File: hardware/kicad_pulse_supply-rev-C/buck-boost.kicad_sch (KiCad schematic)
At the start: 32 parts, among them U12 TPS552892RYQR

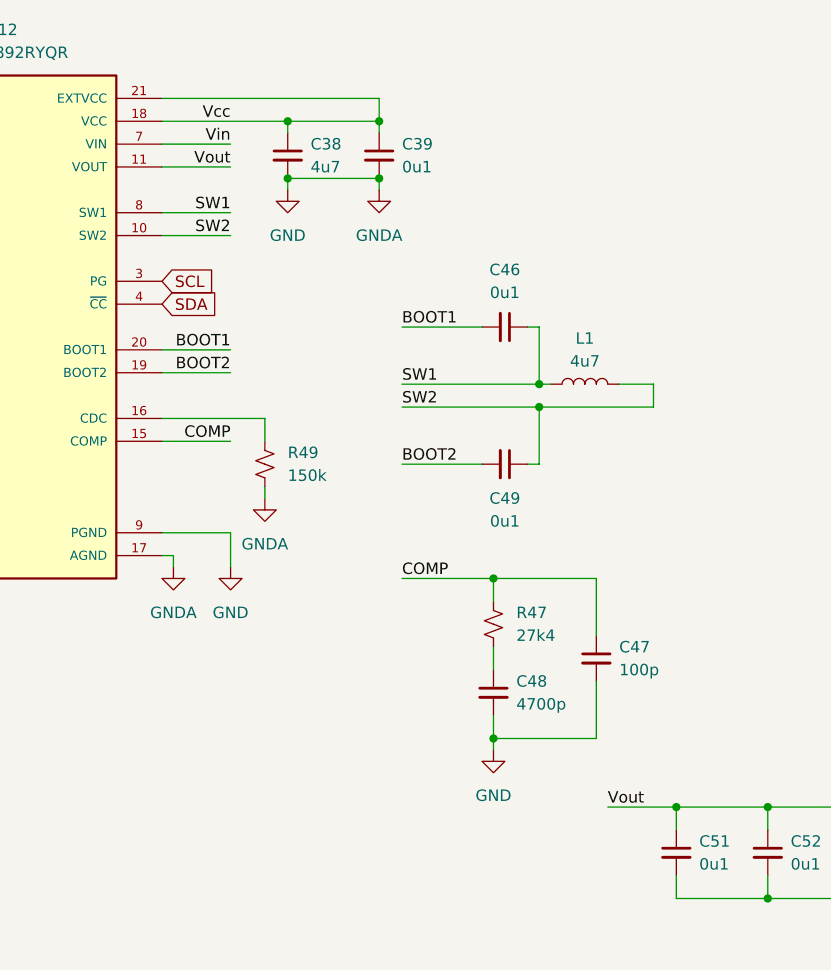
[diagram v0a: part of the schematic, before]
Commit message: Refactored main loop to use Arduino Strings
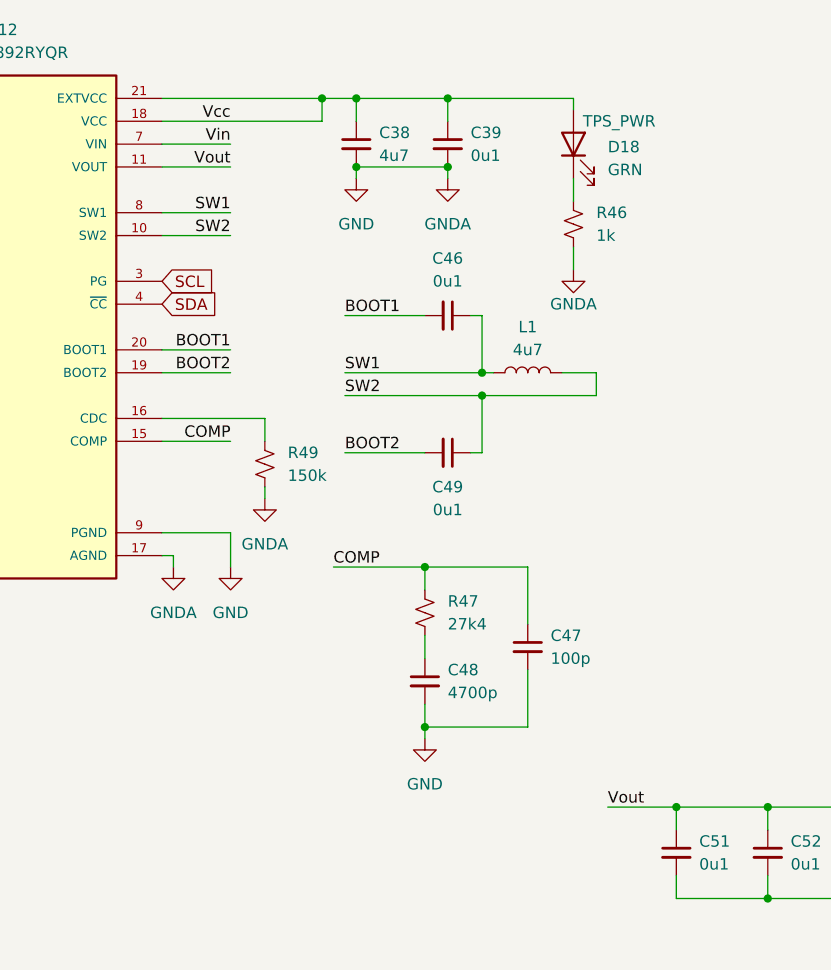
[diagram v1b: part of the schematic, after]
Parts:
- added D18: GRN, symbol Device:LED
- added R46: 1k, symbol Device:R_Small_US
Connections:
- net GND: now also R46.2
- net Vcc: now also D18.2 (A)
- new net: D18.1 (K), R46.1
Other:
- moved on the sheet: C38, C39, C46, C47, C48, C49, L1, R47

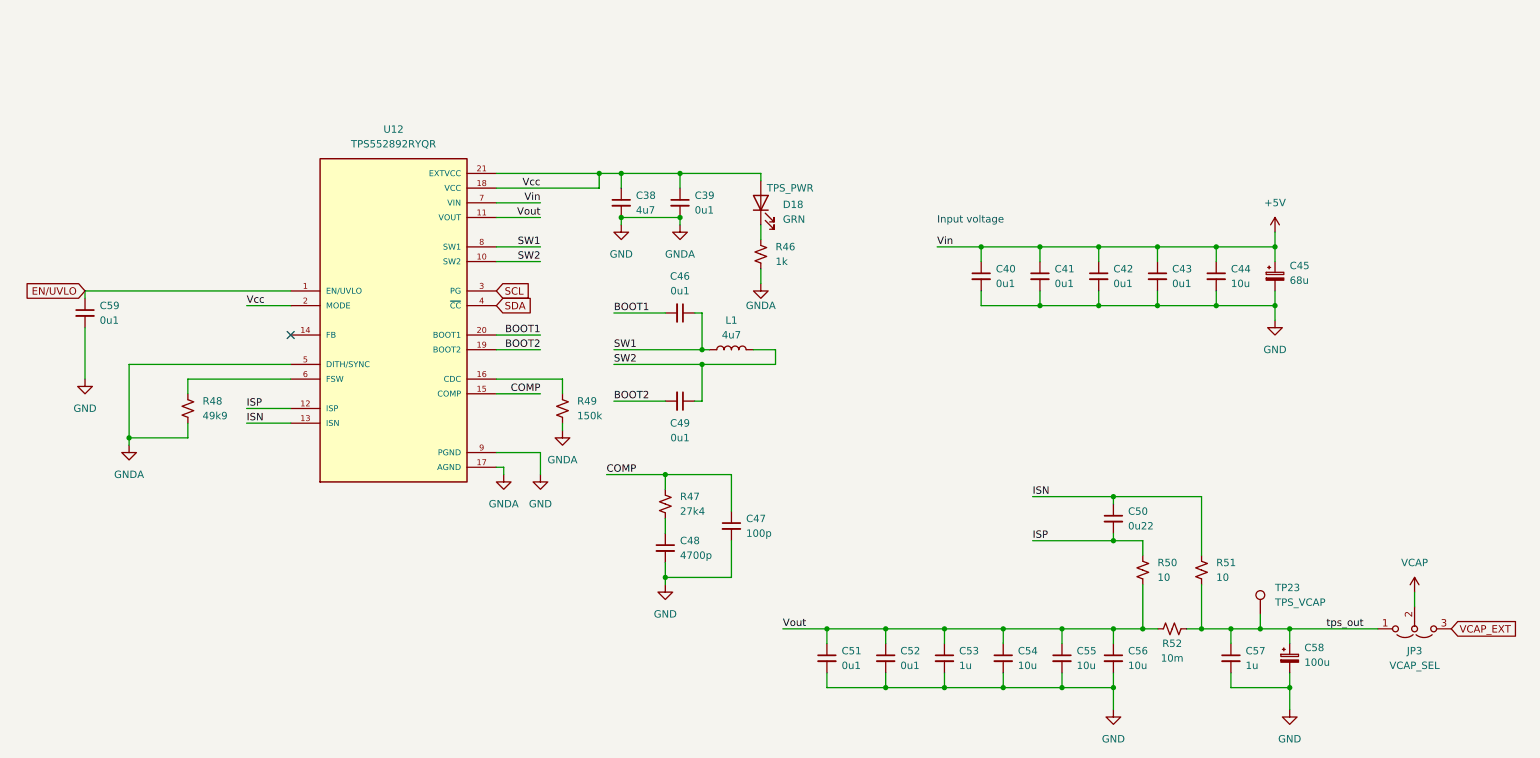
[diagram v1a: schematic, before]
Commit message: hardware breakout boards added, pcb rev-c began
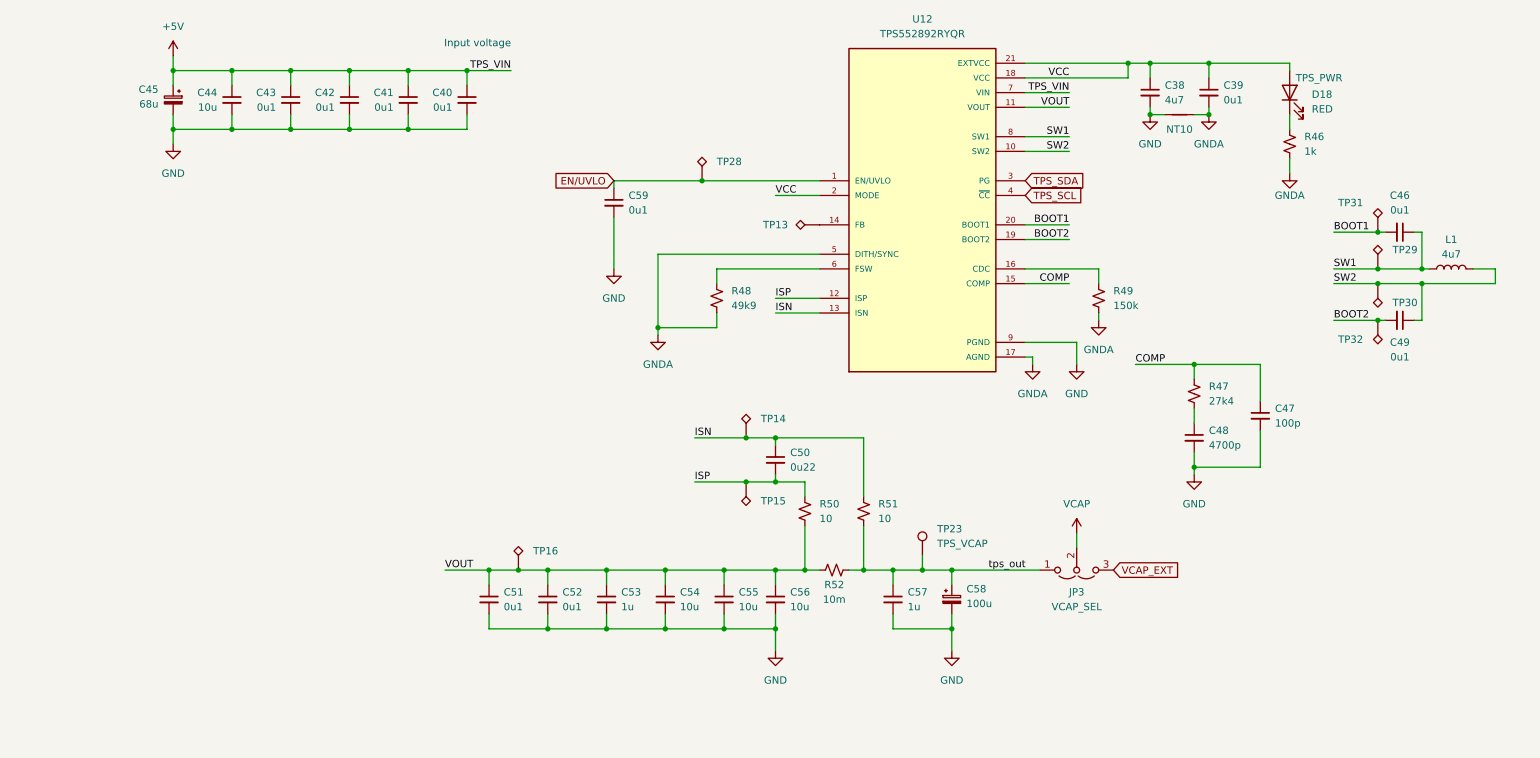
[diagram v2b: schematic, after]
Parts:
- added NT10: ~, symbol Device:NetTie_2
- added TP13, TP14, TP15, TP16, TP28, TP29, TP30, TP31, TP32: ~, symbol Connector:TestPoint_Alt
- D18: value GRN -> RED
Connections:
- net BOOT1: now also TP31.1
- net BOOT2: now also TP32.1
- net EN/UVLO: now also TP28.1
- net GND: now also NT10.1; no longer C39.2, R46.2, R48.2, R49.2, U12.17 (AGND), U12.5 (DITH/SYNC)
- net ISN: now also TP14.1
- net ISP: now also TP15.1
- net SW1: now also TP29.1
- net SW2: now also TP30.1
- net at U12.14 (FB): now also TP13.1
- net SCL renamed TPS_SDA
- net SDA renamed TPS_SCL
- net Vcc renamed VCC
- net Vout renamed VOUT
- net VOUT: now also TP16.1
- new net GNDA: C39.2, NT10.2, R46.2, R48.2, R49.2, U12.17 (AGND), U12.5 (DITH/SYNC)
- no-connect marks 1 -> 0
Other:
- moved on the sheet: C38, C39, C40, C41, C42, C43, C44, C45, C46, C47, C48, C49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
